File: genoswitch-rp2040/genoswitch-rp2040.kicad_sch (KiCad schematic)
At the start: 44 parts, among them J1 USB_B_Micro, J10 RP2040_ADC2, J11 RP2040_ADC3, J2 Conn_01x03_Socket-PicoDebug, J3 HW-SPI0, J4 HW-SPI1, J5 PIO-SPI0, J6 PIO-SPI1, J7 SERIAL, J8 RP2040_ADC0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

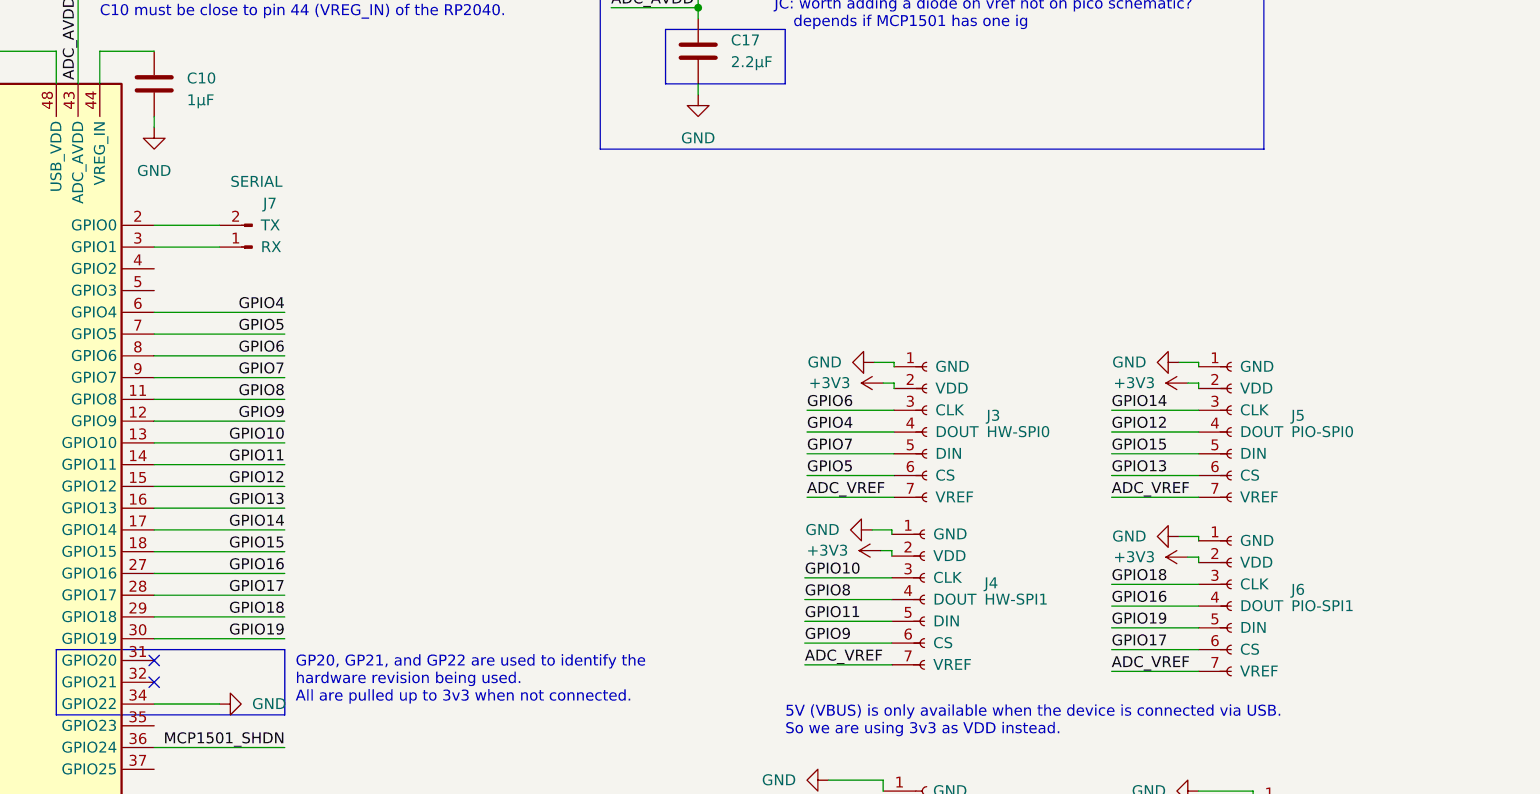
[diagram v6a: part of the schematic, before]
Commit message: Update pinouts for GS connectors -> SPI
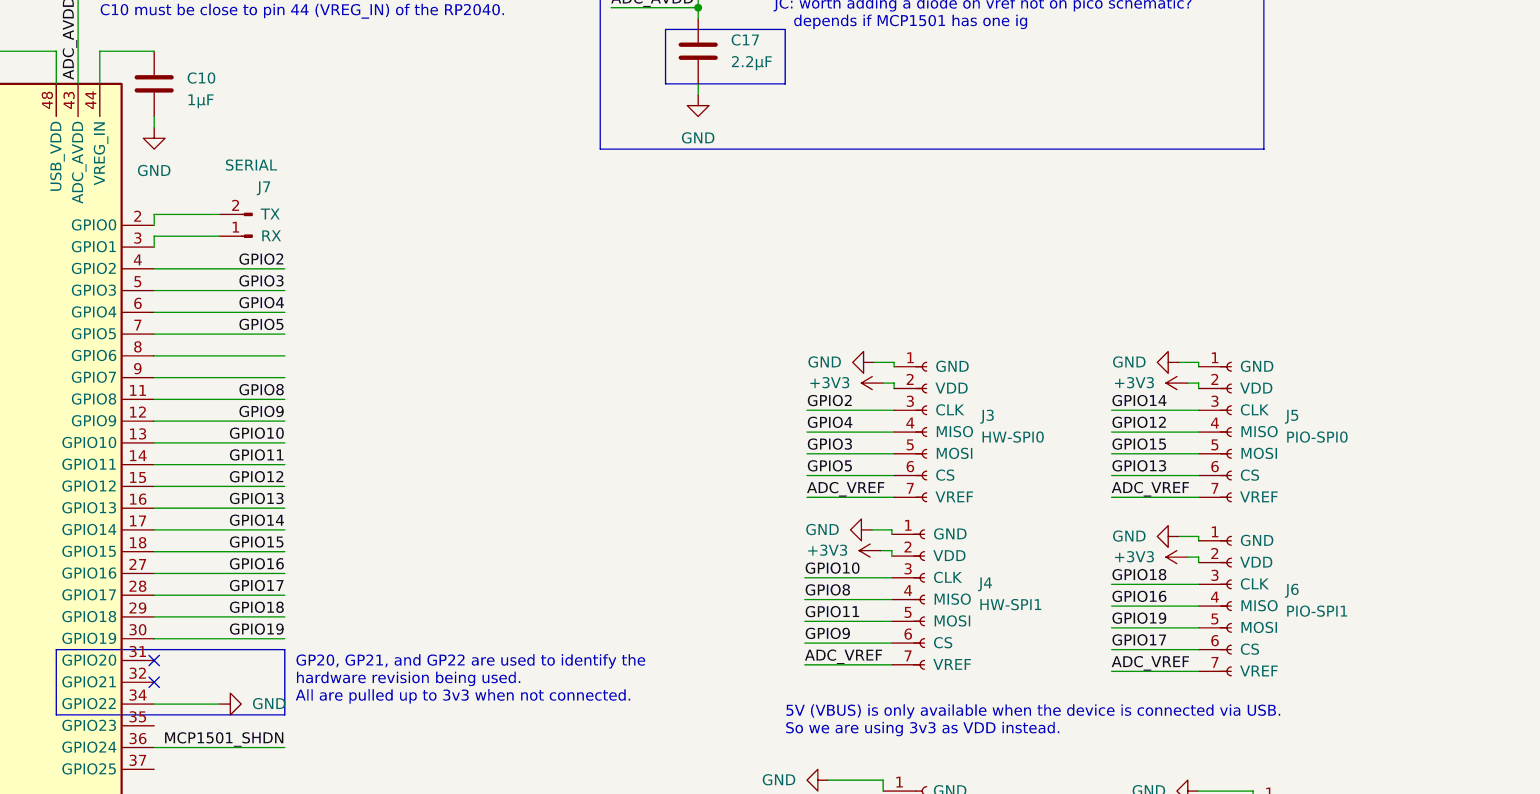
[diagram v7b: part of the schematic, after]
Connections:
- net GPIO2: now reaches U3.4 (GPIO2)
- net GPIO2: now also J3.3 (CLK)
- net GPIO3: now reaches U3.5 (GPIO3)
- net GPIO3: now also J3.5 (MOSI)
- net GPIO6: no longer names the net of U3.8 (GPIO6)
- net GPIO6: no longer J3.3 (CLK)
- net GPIO7: no longer names the net of U3.9 (GPIO7)
- net GPIO7: no longer J3.5 (DIN)
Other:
- moved on the sheet: J7
